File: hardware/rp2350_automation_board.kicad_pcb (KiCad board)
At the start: 2 copper layers, 140 x 105 mm, 114 parts, among them IC1 DAC7562SDGSR, IC2 SN65HVD75DGKR, IC3 LMR51420XFDDCR, J1 PH1-20-UA, J10 TB007-508-02BE, J11 TB007-508-02BE, J12 TB007-508-02BE, J13 39880-0303, J14 TB006-508-03BE, J2 PH1-20-UA, J3 TB006-508-03BE, J4 TB006-508-03BE, J5 TB007-508-02BE, J7 TB006-508-03BE, J9 TB007-508-02BE, Q1 2N7002, Q2 2N7002, Q3 2N7002, Q4 MMBT2907ALT1G, Q5 BSP171PH6327XTSA1, U1 Pico, U10 FUSE_C, U11 LTV-814S-TA1, U12 FUSE_C, U13 TLV9301IDBVR, U14 TLV9301IDBVR, U15 XTR111AIDGQR, U4 FUSE_C, U5 FUSE_C, U6 LTV-814S-TA1, U7 LTV-814S-TA1, U8 FUSE_C, U9 FUSE_C

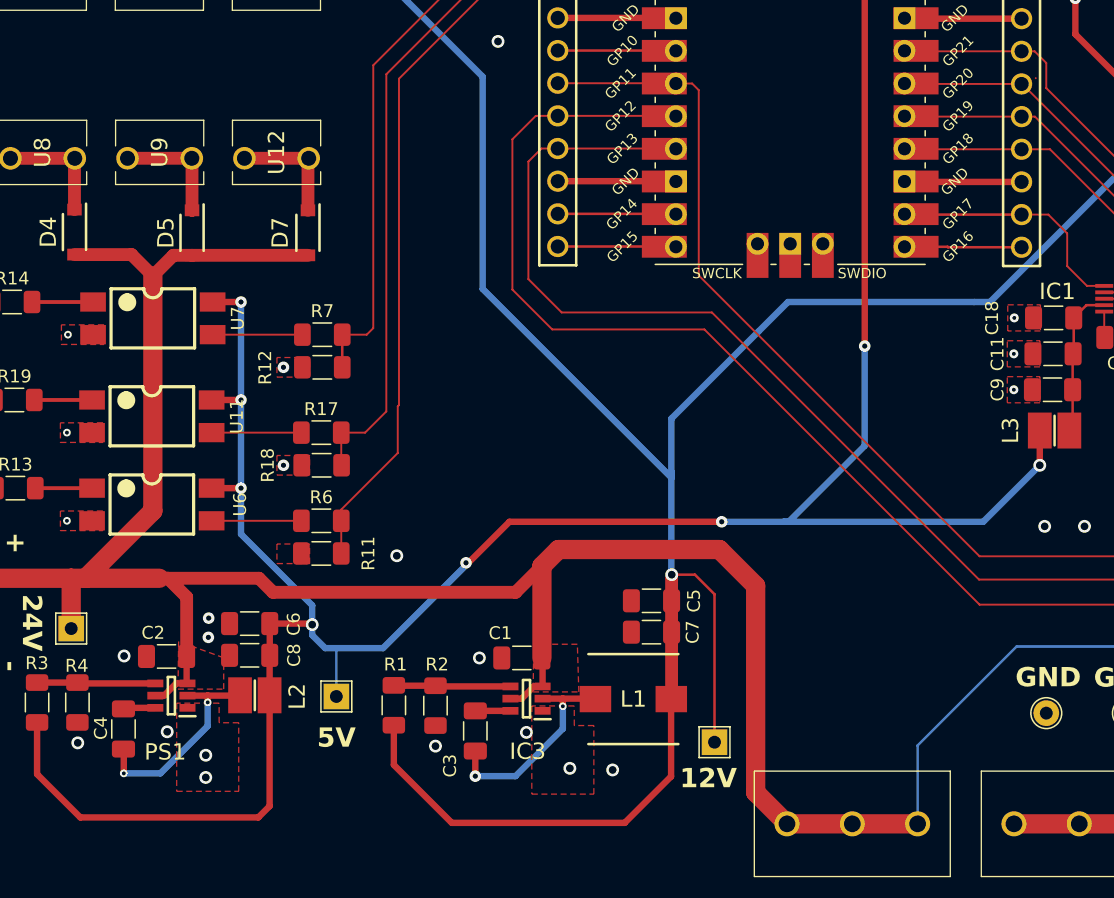
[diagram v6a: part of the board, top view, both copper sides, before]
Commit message: Modbus, small schematic changes
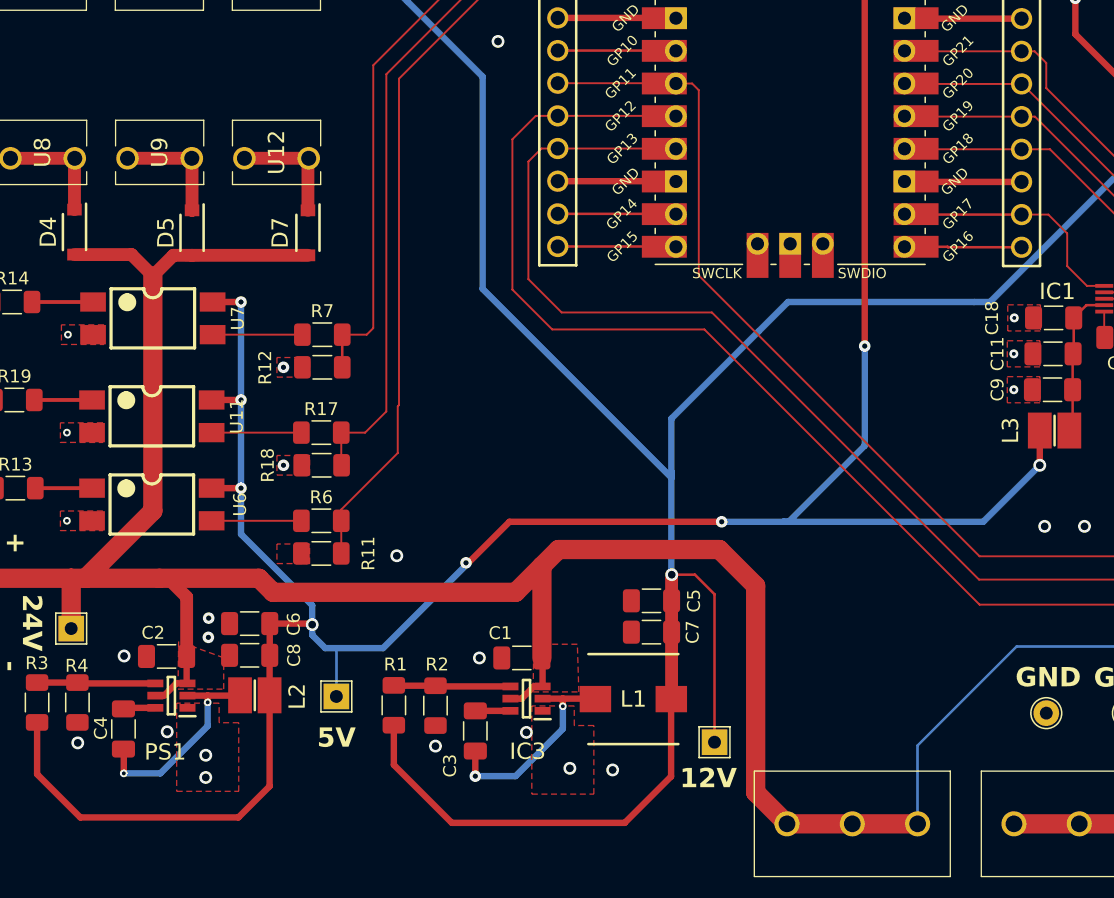
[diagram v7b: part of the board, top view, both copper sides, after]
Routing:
- net +5V: track 243.0 -> 242.0 mm
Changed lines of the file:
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@@
 		(start 74.041 98.7044)
 		(end 75.1332 99.7966)
-		(width 1)
+		(width 1.5)
 		(layer "F.Cu")
 		(net 5)
@@
 		(start 75.1332 99.7966)
 		(end 94.0054 99.7966)
-		(width 1)
+		(width 1.5)
 		(layer "F.Cu")
 		(net 5)
@@
 		(start 94.0054 99.7966)
 		(end 96.0505 97.7515)
-		(width 1)
+		(width 1.5)
 		(layer "F.Cu")
 		(net 5)
@@
 		(start 66.294 98.7044)
 		(end 74.041 98.7044)
-		(width 1)
+		(width 1.5)
 		(layer "F.Cu")
 		(net 5)
@@
 	)
 	(segment
+		(start 72.4424 117.3076)
+		(end 60.1472 117.3076)
+		(width 0.5)
+		(layer "F.Cu")
+		(net 7)
+	)
+	(segment
 		(start 70.358 91.694)
 		(end 72.644 91.694)
@@
 	)
 	(segment
-		(start 74.8678 107.808)
-		(end 74.8678 116.43)
+		(start 56.7814 113.9418)
+		(end 56.7814 109.9168)
 		(width 0.5)
 		(layer "F.Cu")
@@
 	)
 	(segment
-		(start 74.8678 116.43)
-		(end 73.9902 117.3076)
-		(width 0.5)
-		(layer "F.Cu")
-		(net 7)
-	)
-	(segment
 		(start 70.358 84.836)
 		(end 72.644 84.836)
@@
 	)
 	(segment
-		(start 73.9902 117.3076)
-		(end 60.1472 117.3076)
-		(width 0.5)
-		(layer "F.Cu")
-		(net 7)
-	)
-	(segment
 		(start 121.158 40.386)
 		(end 121.158 37.338)
@@
 	)
 	(segment
-		(start 56.7814 113.9418)
-		(end 56.7814 109.9168)
+		(start 74.8678 107.808)
+		(end 74.8678 114.8822)
 		(width 0.5)
 		(layer "F.Cu")
@@
 	)
 	(segment
+		(start 60.1472 117.3076)
+		(end 56.7814 113.9418)
+		(width 0.5)
+		(layer "F.Cu")
+		(net 7)
+	)
+	(segment
 		(start 72.644 77.216)
 		(end 70.436 77.216)
@@
 	)
 	(segment
-		(start 60.1472 117.3076)
-		(end 56.7814 113.9418)
+		(start 74.8678 114.8822)
+		(end 72.4424 117.3076)
 		(width 0.5)
 		(layer "F.Cu")
@@
 		(width 0.15)
 		(layer "F.Cu")
-		(net 96)
-	)
-	(segment
-		(start 134.459702 59.799965)
-		(end 134.459702 59.809102)
-		(width 0.15)
-		(layer "F.Cu")
